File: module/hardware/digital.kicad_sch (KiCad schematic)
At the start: 32 parts

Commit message: Add loopback routing mux; add digital signals to headers
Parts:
- gave numbers to parts that had none: 32

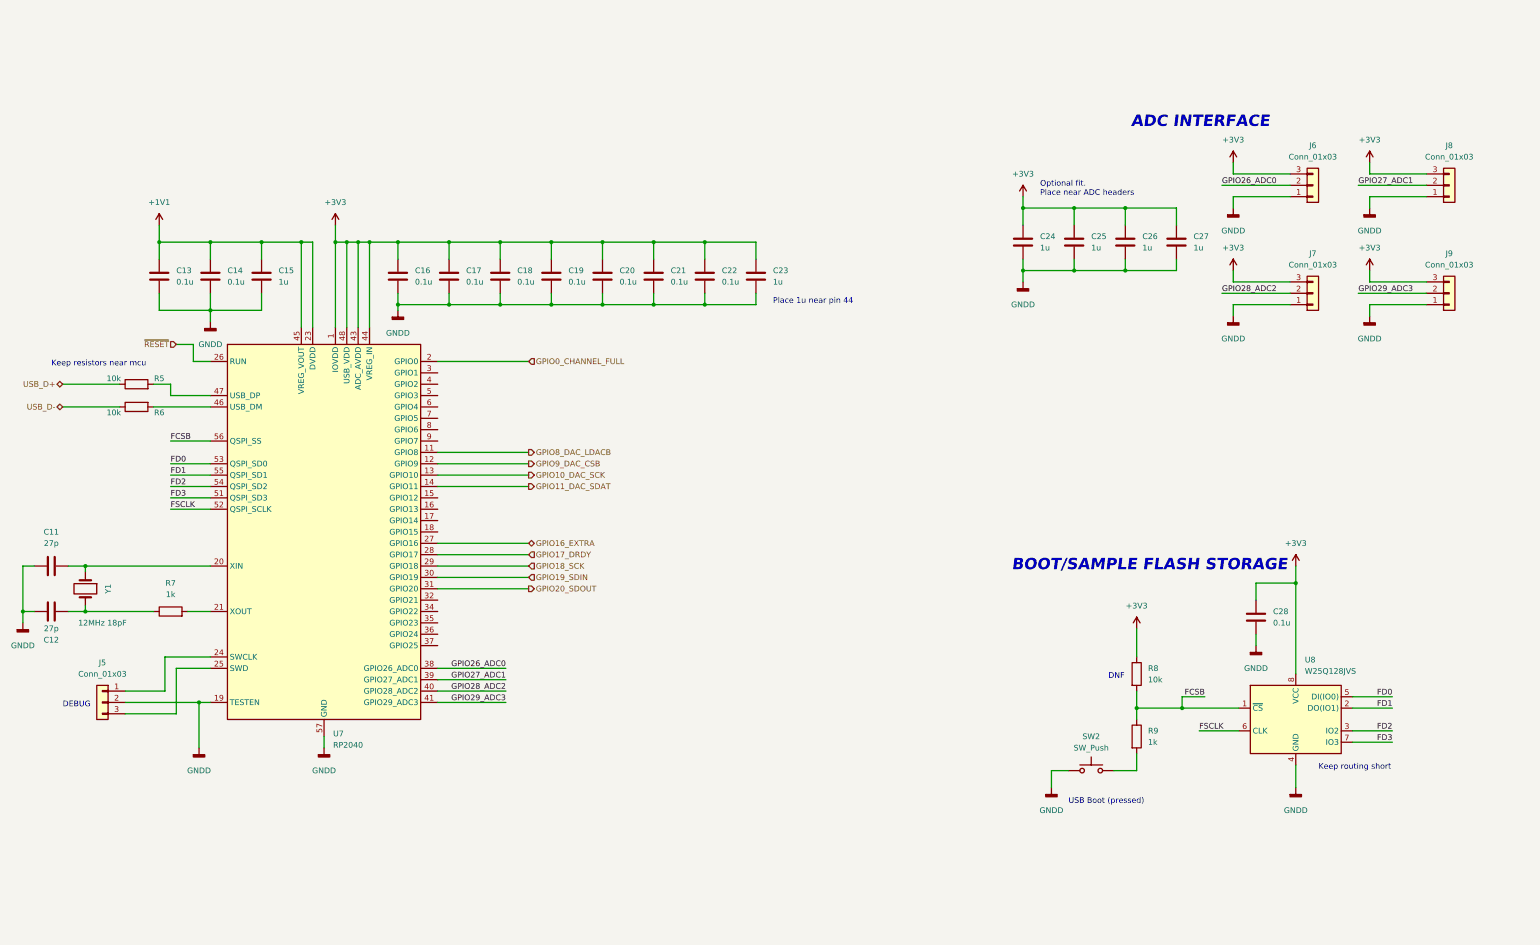
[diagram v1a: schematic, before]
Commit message: Add ADC vref, encoder & button headers
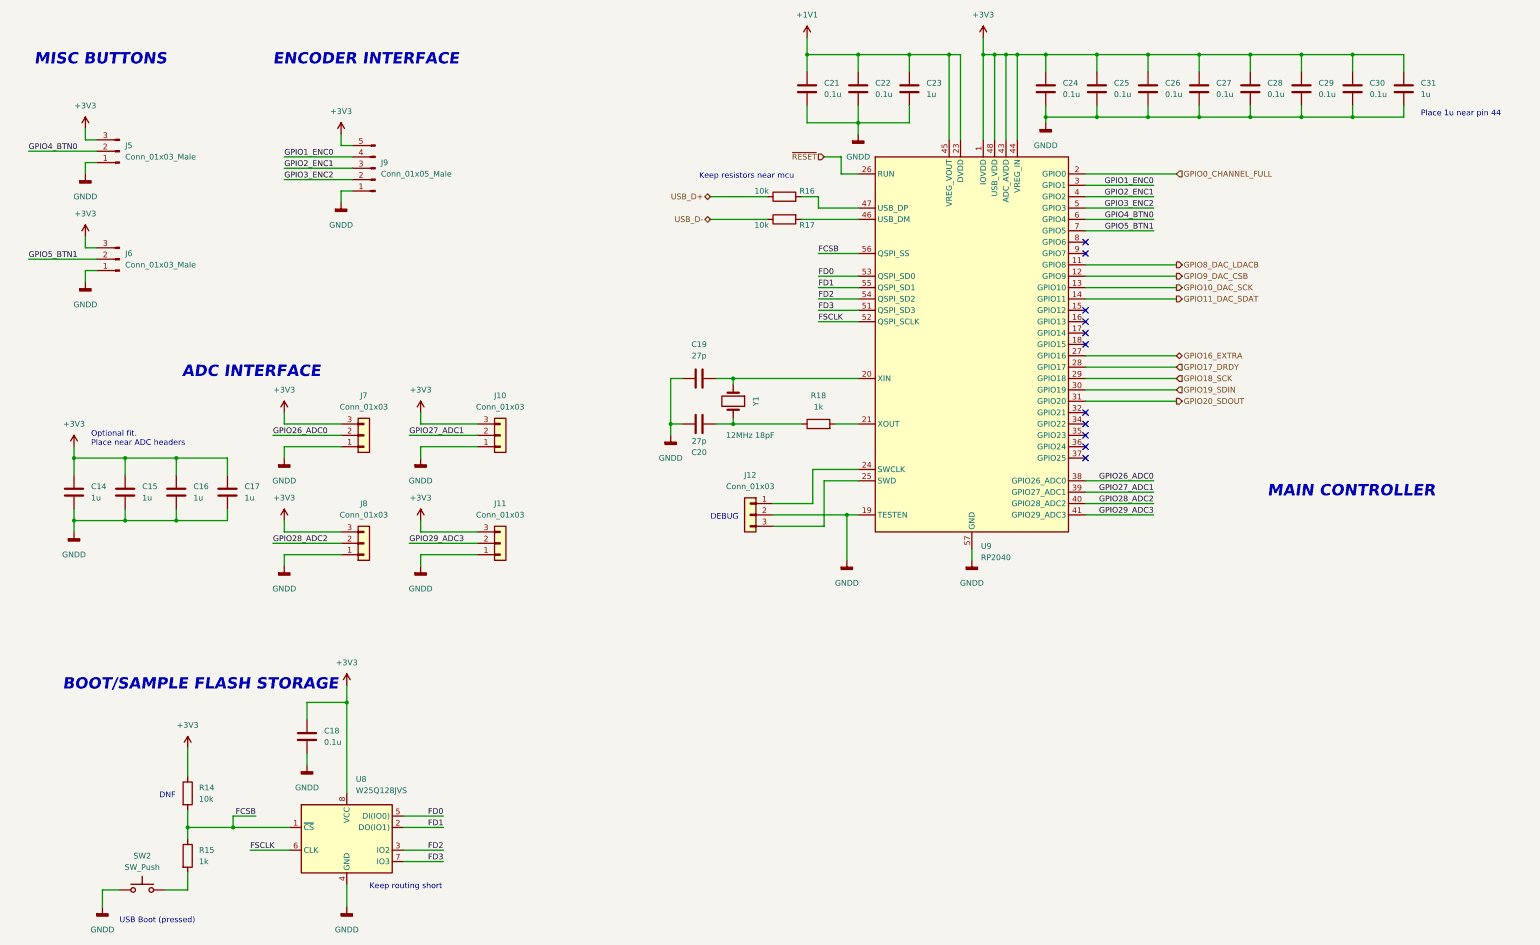
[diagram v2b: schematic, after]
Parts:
- added J5, J6: Conn_01x03_Male, symbol Connector:Conn_01x03_Male
- added J9: Conn_01x05_Male, symbol Connector:Conn_01x05_Male
- renumbered C24 to C14, C25 to C15, C26 to C16, C27 to C17, C28 to C18, C11 to C19, C12 to C20, C13 to C21, C14 to C22, C15 to C23, C16 to C24, C17 to C25, C18 to C26, C19 to C27, C20 to C28, C21 to C29, C22 to C30, C23 to C31, J8 to J10, J9 to J11, J5 to J12, J6 to J7, J7 to J8, R8 to R14, R9 to R15, R5 to R16, R6 to R17, R7 to R18, U7 to U9
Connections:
- net +3V3: now also J5.3 (Pin_3), J6.3 (Pin_3), J9.5 (Pin_5)
- net GNDD: now also J5.1 (Pin_1), J6.1 (Pin_1), J9.1 (Pin_1)
- net GPIO1_ENC0: now reaches U9.3 (GPIO1)
- net GPIO1_ENC0: now also J9.4 (Pin_4)
- net GPIO2_ENC1: now reaches U9.4 (GPIO2)
- net GPIO2_ENC1: now also J9.3 (Pin_3)
- net GPIO3_ENC2: now reaches U9.5 (GPIO3)
- net GPIO3_ENC2: now also J9.2 (Pin_2)
- net GPIO4_BTN0: now reaches U9.6 (GPIO4)
- net GPIO4_BTN0: now also J5.2 (Pin_2)
- net GPIO5_BTN1: now reaches U9.7 (GPIO5)
- net GPIO5_BTN1: now also J6.2 (Pin_2)
- no-connect marks 0 -> 11
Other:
- note added: "ENCODER INTERFACE"
- note added: "MAIN CONTROLLER"
- note added: "MISC BUTTONS"
- moved on the sheet: C14, C15, C16, C17, C18, C19, C20, C21, C22, C23, C24, C25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

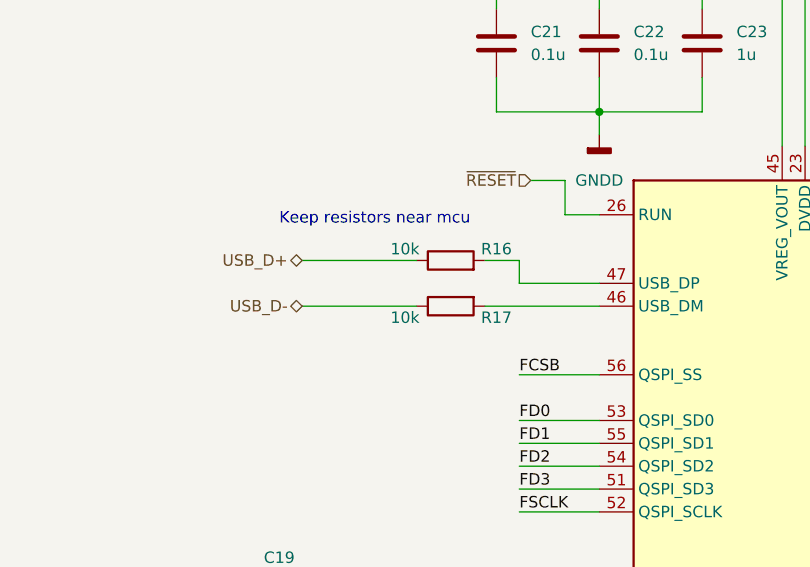
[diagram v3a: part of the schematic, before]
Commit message: Add most footprints
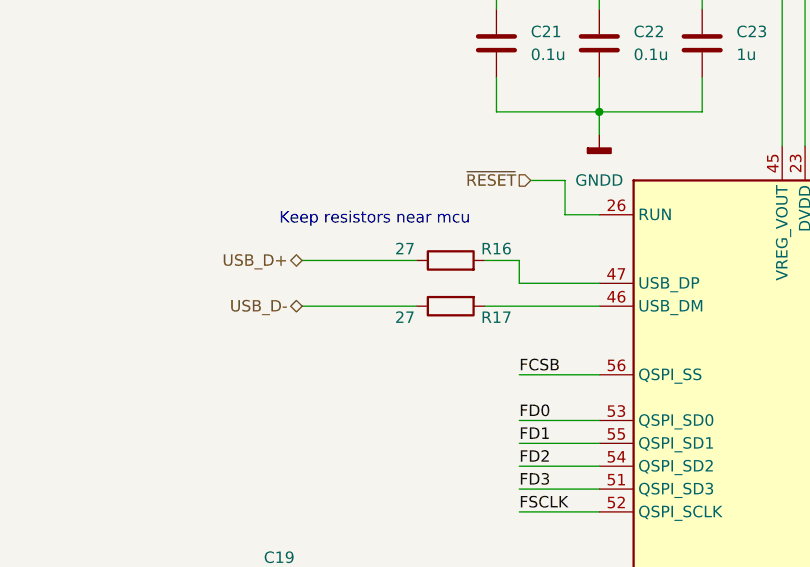
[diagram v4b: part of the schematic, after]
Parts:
- C14, C15, C16, C17, C18, C19, C20, C21, C22, C23, C24, C25, C26, C27, C28, C29, C30, C31: footprint (none) -> Capacitor_SMD:C_0603_1608Metric_Pad1.08x0.95mm_HandSolder
- J10, J11, J12, J5, J6, J7, J8: footprint (none) -> Connector_PinHeader_2.54mm:PinHeader_1x03_P2.54mm_Horizontal
- J9: footprint (none) -> Connector_PinHeader_2.54mm:PinHeader_1x05_P2.54mm_Horizontal
- R14: footprint (none) -> Resistor_SMD:R_0201_0603Metric_Pad0.64x0.40mm_HandSolder
- R15, R18: footprint (none) -> Resistor_SMD:R_0603_1608Metric_Pad0.98x0.95mm_HandSolder
- R16, R17: value 10k -> 27; footprint (none) -> Resistor_SMD:R_0603_1608Metric_Pad0.98x0.95mm_HandSolder
- Y1: footprint (none) -> Crystal:Crystal_SMD_HC49-SD

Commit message: Finish footprint assignments; create cusom footprint lib
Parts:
- SW2: footprint (none) -> custom:TE_ConnMSLPT5252CG1
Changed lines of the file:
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@@
     (property "Reference" "SW2" (id 0) (at 82.55 219.71 0))
     (property "Value" "SW_Push" (id 1) (at 82.55 222.25 0))
-    (property "Footprint" "" (id 2) (at 82.55 222.25 0)
+    (property "Footprint" "custom:TE_ConnMSLPT5252CG1" (id 2) (at 82.55 222.25 0)
       (effects (font (size 1.27 1.27)) hide)
     )

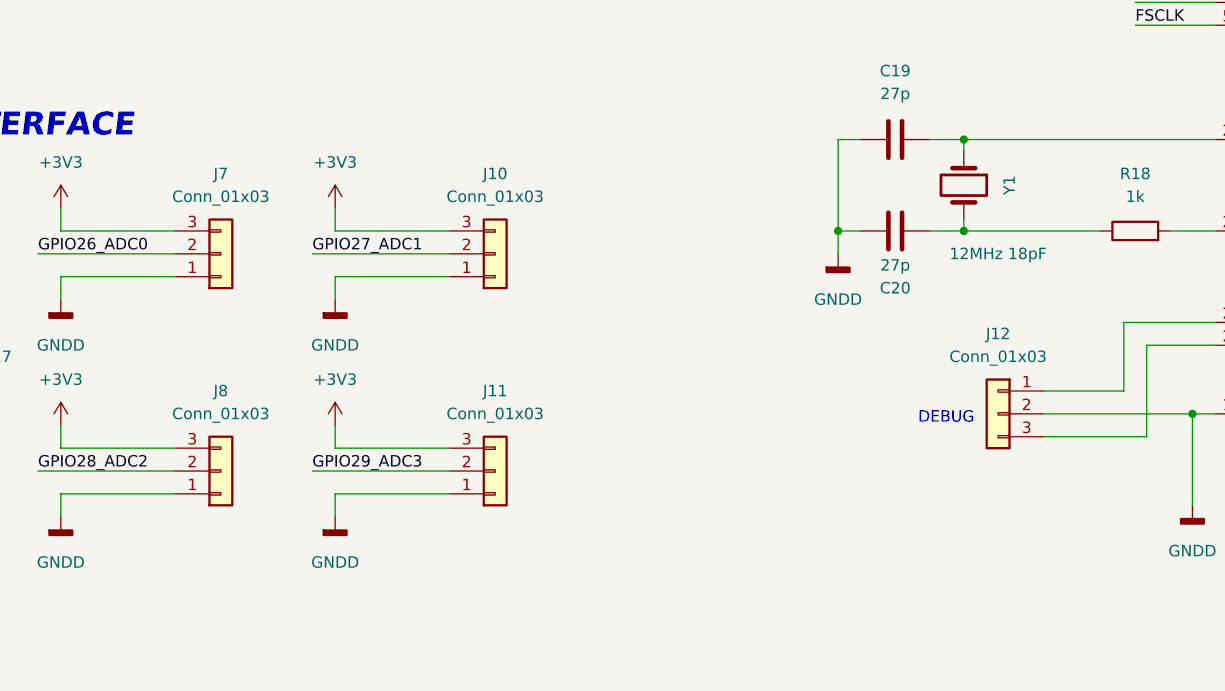
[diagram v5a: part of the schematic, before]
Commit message: Fix header footprints
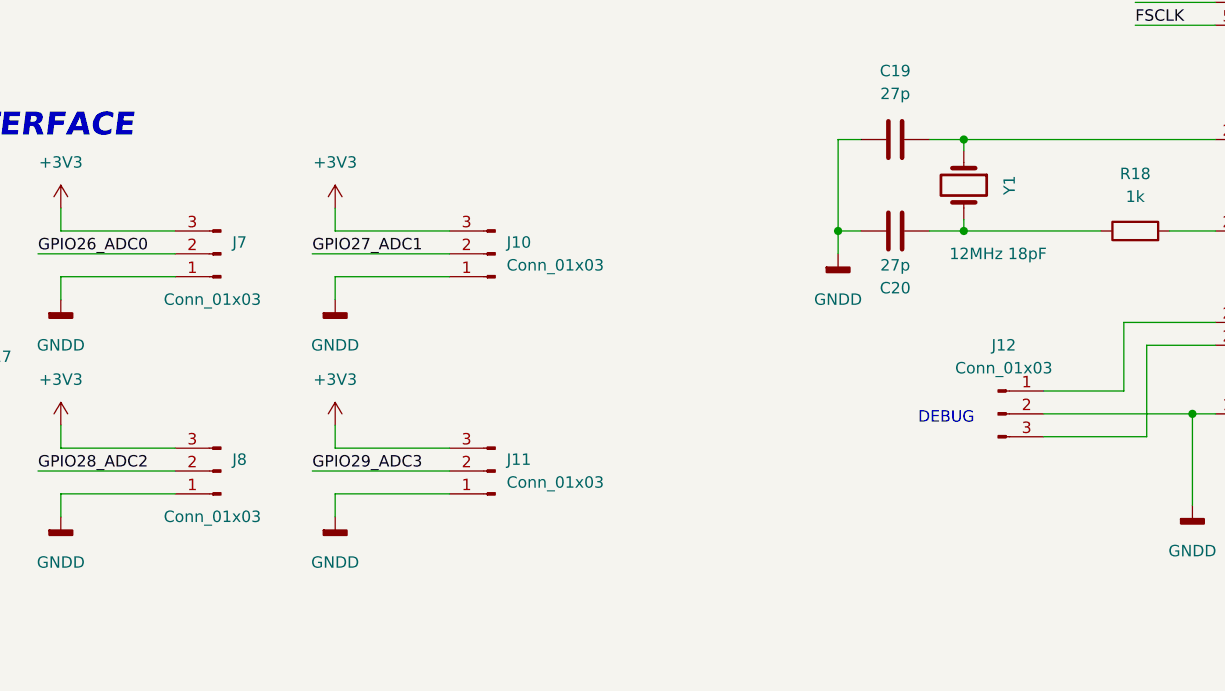
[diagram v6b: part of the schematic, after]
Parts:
- J10, J11, J12, J7, J8: footprint Connector_PinHeader_2.54mm:PinHeader_1x03_P2.54mm_Horizontal -> Connector_PinHeader_2.54mm:PinHeader_1x03_P2.54mm_Vertical; symbol Connector_Generic:Conn_01x03 -> Connector:Conn_01x03_Male
- J5, J6: footprint Connector_PinHeader_2.54mm:PinHeader_1x03_P2.54mm_Horizontal -> Connector_PinHeader_2.54mm:PinHeader_1x03_P2.54mm_Vertical
- J9: footprint Connector_PinHeader_2.54mm:PinHeader_1x05_P2.54mm_Horizontal -> Connector_PinHeader_2.54mm:PinHeader_1x05_P2.54mm_Vertical
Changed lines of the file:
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@@
     (effects (font (size 1.27 1.27)) (justify left))
   )
-  (symbol (lib_id "Connector_Generic:Conn_01x03") (at 132.08 125.73 0) (mirror x) (unit 1)
-    (in_bom yes) (on_board yes) (fields_autoplaced)
-    (property "Reference" "J7" (id 0) (at 132.08 116.84 0))
-    (property "Value" "Conn_01x03" (id 1) (at 132.08 119.38 0))
-    (property "Footprint" "Connector_PinHeader_2.54mm:PinHeader_1x03_P2.54mm_Horizontal" (id 2) (at 132.08 125.73 0)
+  (symbol (lib_id "Connector:Conn_01x03_Male") (at 132.08 125.73 180) (unit 1)
+    (in_bom yes) (on_board yes)
+    (property "Reference" "J7" (id 0) (at 133.35 124.4599 0)
+      (effects (font (size 1.27 1.27)) (justify right))
+    )
+    (property "Value" "Conn_01x03" (id 1) (at 125.73 130.81 0)
+      (effects (font (size 1.27 1.27)) (justify right))
+    )
+    (property "Footprint" "Connector_PinHeader_2.54mm:PinHeader_1x03_P2.54mm_Vertical" (id 2) (at 132.08 125.73 0)
       (effects (font (size 1.27 1.27)) hide)
     )
@@
       (effects (font (size 1.27 1.27)) (justify right))
     )
-    (property "Footprint" "Connector_PinHeader_2.54mm:PinHeader_1x03_P2.54mm_Horizontal" (id 2) (at 77.47 62.23 0)
+    (property "Footprint" "Connector_PinHeader_2.54mm:PinHeader_1x03_P2.54mm_Vertical" (id 2) (at 77.47 62.23 0)
       (effects (font (size 1.27 1.27)) hide)
     )
@@
       (effects (font (size 1.27 1.27)) (justify right))
     )
-    (property "Footprint" "Connector_PinHeader_2.54mm:PinHeader_1x03_P2.54mm_Horizontal" (id 2) (at 77.47 86.36 0)
+    (property "Footprint" "Connector_PinHeader_2.54mm:PinHeader_1x03_P2.54mm_Vertical" (id 2) (at 77.47 86.36 0)
       (effects (font (size 1.27 1.27)) hide)
     )
@@
     (pin "1")
   )
-  (symbol (lib_id "Connector_Generic:Conn_01x03") (at 218.44 143.51 0) (mirror y) (unit 1)
-    (in_bom yes) (on_board yes) (fields_autoplaced)
-    (property "Reference" "J12" (id 0) (at 218.44 134.62 0))
-    (property "Value" "Conn_01x03" (id 1) (at 218.44 137.16 0))
-    (property "Footprint" "Connector_PinHeader_2.54mm:PinHeader_1x03_P2.54mm_Horizontal" (id 2) (at 218.44 143.51 0)
+  (symbol (lib_id "Connector:Conn_01x03_Male") (at 218.44 143.51 0) (unit 1)
+    (in_bom yes) (on_board yes) (fields_autoplaced)
+    (property "Reference" "J12" (id 0) (at 219.075 135.89 0))
+    (property "Value" "Conn_01x03" (id 1) (at 219.075 138.43 0))
+    (property "Footprint" "Connector_PinHeader_2.54mm:PinHeader_1x03_P2.54mm_Vertical" (id 2) (at 218.44 143.51 0)
       (effects (font (size 1.27 1.27)) hide)
     )
@@
     (pin "2")
   )
-  (symbol (lib_id "Connector_Generic:Conn_01x03") (at 162.56 125.73 0) (mirror x) (unit 1)
-    (in_bom yes) (on_board yes) (fields_autoplaced)
-    (property "Reference" "J10" (id 0) (at 162.56 116.84 0))
-    (property "Value" "Conn_01x03" (id 1) (at 162.56 119.38 0))
-    (property "Footprint" "Connector_PinHeader_2.54mm:PinHeader_1x03_P2.54mm_Horizontal" (id 2) (at 162.56 125.73 0)
+  (symbol (lib_id "Connector:Conn_01x03_Male") (at 162.56 125.73 180) (unit 1)
+    (in_bom yes) (on_board yes) (fields_autoplaced)
+    (property "Reference" "J10" (id 0) (at 163.83 124.4599 0)
+      (effects (font (size 1.27 1.27)) (justify right))
+    )
+    (property "Value" "Conn_01x03" (id 1) (at 163.83 126.9999 0)
+      (effects (font (size 1.27 1.27)) (justify right))
+    )
+    (property "Footprint" "Connector_PinHeader_2.54mm:PinHeader_1x03_P2.54mm_Vertical" (id 2) (at 162.56 125.73 0)
       (effects (font (size 1.27 1.27)) hide)
     )
@@
     (pin "2")
   )
-  (symbol (lib_id "Connector_Generic:Conn_01x03") (at 162.56 149.86 0) (mirror x) (unit 1)
-    (in_bom yes) (on_board yes) (fields_autoplaced)
-    (property "Reference" "J11" (id 0) (at 162.56 140.97 0))
-    (property "Value" "Conn_01x03" (id 1) (at 162.56 143.51 0))
-    (property "Footprint" "Connector_PinHeader_2.54mm:PinHeader_1x03_P2.54mm_Horizontal" (id 2) (at 162.56 149.86 0)
+  (symbol (lib_id "Connector:Conn_01x03_Male") (at 162.56 149.86 180) (unit 1)
+    (in_bom yes) (on_board yes) (fields_autoplaced)
+    (property "Reference" "J11" (id 0) (at 163.83 148.5899 0)
+      (effects (font (size 1.27 1.27)) (justify right))
+    )
+    (property "Value" "Conn_01x03" (id 1) (at 163.83 151.1299 0)
+      (effects (font (size 1.27 1.27)) (justify right))
+    )
+    (property "Footprint" "Connector_PinHeader_2.54mm:PinHeader_1x03_P2.54mm_Vertical" (id 2) (at 162.56 149.86 0)
       (effects (font (size 1.27 1.27)) hide)
     )
@@
     (pin "1")
   )
-  (symbol (lib_id "Connector_Generic:Conn_01x03") (at 132.08 149.86 0) (mirror x) (unit 1)
-    (in_bom yes) (on_board yes) (fields_autoplaced)
-    (property "Reference" "J8" (id 0) (at 132.08 140.97 0))
-    (property "Value" "Conn_01x03" (id 1) (at 132.08 143.51 0))
-    (property "Footprint" "Connector_PinHeader_2.54mm:PinHeader_1x03_P2.54mm_Horizontal" (id 2) (at 132.08 149.86 0)
+  (symbol (lib_id "Connector:Conn_01x03_Male") (at 132.08 149.86 180) (unit 1)
+    (in_bom yes) (on_board yes)
+    (property "Reference" "J8" (id 0) (at 133.35 148.5899 0)
+      (effects (font (size 1.27 1.27)) (justify right))
+    )
+    (property "Value" "Conn_01x03" (id 1) (at 125.73 154.94 0)
+      (effects (font (size 1.27 1.27)) (justify right))
+    )
+    (property "Footprint" "Connector_PinHeader_2.54mm:PinHeader_1x03_P2.54mm_Vertical" (id 2) (at 132.08 149.86 0)
       (effects (font (size 1.27 1.27)) hide)
     )
@@
       (effects (font (size 1.27 1.27)) (justify right))
     )
-    (property "Footprint" "Connector_PinHeader_2.54mm:PinHeader_1x05_P2.54mm_Horizontal" (id 2) (at 134.62 66.04 0)
-      (effects (font (size 1.27 1.27)) hide)
-    )
+    (property "Footprint" "Connector_PinHeader_2.54mm:PinHeader_1x05_P2.54mm_Vertical" (id 2) (at 134.62 66.04 0)
+      (effects (font (size 1.27 1.27)) hide)
+    )

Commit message: Begin layout process for module
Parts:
- R14: footprint Resistor_SMD:R_0201_0603Metric_Pad0.64x0.40mm_HandSolder -> Resistor_SMD:R_0603_1608Metric_Pad0.98x0.95mm_HandSolder
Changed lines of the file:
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@@
       (effects (font (size 1.27 1.27)) (justify left))
     )
-    (property "Footprint" "Resistor_SMD:R_0201_0603Metric_Pad0.64x0.40mm_HandSolder" (id 2) (at 90.932 205.74 90)
+    (property "Footprint" "Resistor_SMD:R_0603_1608Metric_Pad0.98x0.95mm_HandSolder" (id 2) (at 90.932 205.74 90)
       (effects (font (size 1.27 1.27)) hide)
     )
